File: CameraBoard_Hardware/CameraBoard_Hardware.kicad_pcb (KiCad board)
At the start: 2 copper layers, 61 x 100 mm, 39 parts, among them J1 CAM_OUT0, J2 CAM_OUT1, U1 TM4C129E_Launchpad, U2 AP1059, U3 MAX4314ESD+, U4 MAX4314ESD+

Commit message: Added BOM, added LED for +5V power
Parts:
- added D7: LED, LEDs:LED_0603_HandSoldering, F.Cu at (97.0, 97.1)
- added R14: 500, Resistors_SMD:R_0603_HandSoldering, F.Cu at (97.0, 104.3)
- J1: value CAM_OUT0 -> BNC_75_OHM_HORIZ
- J2: value CAM_OUT1 -> BNC_75_OHM_HORIZ
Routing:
- net +5V: track 100.4 -> 114.1 mm
- net Net-(D7-Pad1): track 0.00 -> 5.02 mm
- net GND: vias 3 -> 7
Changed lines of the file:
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@@
   (general
     (thickness 1.6)
-    (drawings 30)
-    (tracks 226)
+    (drawings 31)
+    (tracks 234)
     (zones 0)
-    (modules 39)
-    (nets 64)
+    (modules 41)
+    (nets 65)
   )
   (page A4)
@@
   )
   (setup
-    (last_trace_width 0.25)
+    (last_trace_width 0.381)
     (user_trace_width 0.254)
     (user_trace_width 0.381)
@@
   (net 62 "Net-(U1-Pad+3V3)")
   (net 63 +10V)
+  (net 64 "Net-(D7-Pad1)")
   (net_class Default "This is the default net class."
     (clearance 0.2)
@@
     (add_net "Net-(D5-Pad1)")
     (add_net "Net-(D6-Pad1)")
+    (add_net "Net-(D7-Pad1)")
     (add_net "Net-(J1-Pad2)")
     (add_net "Net-(J2-Pad2)")
@@
       (effects (font (size 1 1) (thickness 0.15)))
     )
-    (fp_text value CAM_OUT0 (at 2.3622 2.0828) (layer F.SilkS)
+    (fp_text value BNC_75_OHM_HORIZ (at 2.3622 2.0828) (layer F.SilkS)
       (effects (font (size 1 1) (thickness 0.15)))
     )
@@
       (effects (font (size 1 1) (thickness 0.15)))
     )
-    (fp_text value CAM_OUT1 (at 2.3876 2.0828) (layer F.SilkS)
+    (fp_text value BNC_75_OHM_HORIZ (at 2.3876 2.0828) (layer F.SilkS)
       (effects (font (size 1 1) (thickness 0.15)))
     )
@@
       (xy 3.076472 -5.52068) (xy 3.111284 -5.541334) (xy 3.12377 -5.541189)) (layer F.SilkS) (width 0.01))
   )
+  (module LEDs:LED_0603_HandSoldering (layer F.Cu)
+    (at 97.028 97.0866 90)
+    (descr "LED SMD 0603, hand soldering")
+    (tags "LED 0603")
+    (attr smd)
+    (fp_text reference D7 (at 2.9034 0 90) (layer F.SilkS)
+      (effects (font (size 1 1) (thickness 0.15)))
+    )
+    (fp_text value LED (at 0 1.55 90) (layer F.Fab)
+      (effects (font (size 1 1) (thickness 0.15)))
+    )
+    (fp_line (start -0.8 -0.4) (end -0.8 0.4) (layer F.Fab) (width 0.1))
+    (fp_line (start 1.95 0.7) (end -1.96 0.7) (layer F.CrtYd) (width 0.05))
+    (fp_line (start 1.95 0.7) (end 1.95 -0.7) (layer F.CrtYd) (width 0.05))
+    (fp_line (start -1.96 -0.7) (end -1.96 0.7) (layer F.CrtYd) (width 0.05))
+    (fp_line (start -1.96 -0.7) (end 1.95 -0.7) (layer F.CrtYd) (width 0.05))
+    (fp_line (start -1.8 -0.55) (end 0.8 -0.55) (layer F.SilkS) (width 0.12))
+    (fp_line (start -1.8 0.55) (end 0.8 0.55) (layer F.SilkS) (width 0.12))
+    (fp_line (start -0.8 -0.4) (end 0.8 -0.4) (layer F.Fab) (width 0.1))
+    (fp_line (start 0.8 -0.4) (end 0.8 0.4) (layer F.Fab) (width 0.1))
+    (fp_line (start 0.8 0.4) (end -0.8 0.4) (layer F.Fab) (width 0.1))
+    (fp_line (start 0.15 -0.2) (end 0.15 0.2) (layer F.Fab) (width 0.1))
+    (fp_line (start 0.15 0.2) (end -0.15 0) (layer F.Fab) (width 0.1))
+    (fp_line (start -0.15 0) (end 0.15 -0.2) (layer F.Fab) (width 0.1))
+    (fp_line (start -0.2 -0.2) (end -0.2 0.2) (layer F.Fab) (width 0.1))
+    (fp_line (start -1.8 -0.55) (end -1.8 0.55) (layer F.SilkS) (width 0.12))
+    (pad 2 smd rect (at 1.1 0 90) (size 1.2 0.9) (layers F.Cu F.Paste F.Mask)
+      (net 57 +5V))
+    (pad 1 smd rect (at -1.1 0 90) (size 1.2 0.9) (layers F.Cu F.Paste F.Mask)
+      (net 64 "Net-(D7-Pad1)"))
+    (model ${KISYS3DMOD}/LEDs.3dshapes/LED_0603.wrl
+      (at (xyz 0 0 0))
+      (scale (xyz 1 1 1))
+      (rotate (xyz 0 0 180))
+    )
+  )
+  (module Resistors_SMD:R_0603_HandSoldering (layer F.Cu)
+    (at 97.028 104.31 270)
+    (descr "Resistor SMD 0603, hand soldering")
+    (tags "resistor 0603")
+    (attr smd)
+    (fp_text reference R14 (at -3.3704 -0.0254 270) (layer F.SilkS)
+      (effects (font (size 1 1) (thickness 0.15)))
+    )
+    (fp_text value 500 (at 0 1.55 270) (layer F.Fab)
+      (effects (font (size 1 1) (thickness 0.15)))
+    )
+    (fp_line (start 1.95 0.7) (end -1.96 0.7) (layer F.CrtYd) (width 0.05))
+    (fp_line (start 1.95 0.7) (end 1.95 -0.7) (layer F.CrtYd) (width 0.05))
+    (fp_line (start -1.96 -0.7) (end -1.96 0.7) (layer F.CrtYd) (width 0.05))
+    (fp_line (start -1.96 -0.7) (end 1.95 -0.7) (layer F.CrtYd) (width 0.05))
+    (fp_line (start -0.5 -0.68) (end 0.5 -0.68) (layer F.SilkS) (width 0.12))
+    (fp_line (start 0.5 0.68) (end -0.5 0.68) (layer F.SilkS) (width 0.12))
+    (fp_line (start -0.8 -0.4) (end 0.8 -0.4) (layer F.Fab) (width 0.1))
+    (fp_line (start 0.8 -0.4) (end 0.8 0.4) (layer F.Fab) (width 0.1))
+    (fp_line (start 0.8 0.4) (end -0.8 0.4) (layer F.Fab) (width 0.1))
+    (fp_line (start -0.8 0.4) (end -0.8 -0.4) (layer F.Fab) (width 0.1))
+    (fp_text user %R (at 0 0 270) (layer F.Fab)
+      (effects (font (size 0.4 0.4) (thickness 0.075)))
+    )
+    (pad 2 smd rect (at 1.1 0 270) (size 1.2 0.9) (layers F.Cu F.Paste F.Mask)
+      (net 2 GND))
+    (pad 1 smd rect (at -1.1 0 270) (size 1.2 0.9) (layers F.Cu F.Paste F.Mask)
+      (net 64 "Net-(D7-Pad1)"))
+    (model ${KISYS3DMOD}/Resistors_SMD.3dshapes/R_0603.wrl
+      (at (xyz 0 0 0))
+      (scale (xyz 1 1 1))
+      (rotate (xyz 0 0 0))
+    )
+  )
+  (gr_text +5V (at 97.0788 107.9754 90) (layer F.SilkS)
+    (effects (font (size 1 1) (thickness 0.15)))
+  )
   (gr_text +10V (at 127.0254 62.23) (layer F.SilkS)
     (effects (font (size 1.5 1.5) (thickness 0.3)))
@@
   (segment (start 126.2736 101.3968) (end 126.2736 101.2088) (width 0.381) (layer F.Cu) (net 2))
   (via (at 124.6378 99.3648) (size 0.8) (drill 0.4) (layers F.Cu B.Cu) (net 2))
+  (via (at 100.1268 101.2698) (size 0.8) (drill 0.4) (layers F.Cu B.Cu) (net 2))
+  (via (at 101.4476 102.6668) (size 0.8) (drill 0.4) (layers F.Cu B.Cu) (net 2))
+  (via (at 103.4288 100.3554) (size 0.8) (drill 0.4) (layers F.Cu B.Cu) (net 2))
+  (via (at 102.2858 99.1616) (size 0.8) (drill 0.4) (layers F.Cu B.Cu) (net 2))
   (via (at 130.4544 91.8972) (size 0.8) (drill 0.4) (layers F.Cu B.Cu) (net 3))
   (segment (start 127.0762 91.9226) (end 130.429 91.9226) (width 0.381) (layer F.Cu) (net 3))
@@
   (segment (start 106.8578 105.3338) (end 121.793 105.3338) (width 0.381) (layer B.Cu) (net 57))
   (segment (start 106.4006 105.791) (end 106.8578 105.3338) (width 0.381) (layer B.Cu) (net 57))
+  (segment (start 106.4006 105.5092) (end 106.4006 105.791) (width 0.381) (layer F.Cu) (net 57))
+  (segment (start 97.028 96.1366) (end 106.4006 105.5092) (width 0.381) (layer F.Cu) (net 57))
+  (segment (start 97.028 95.9866) (end 97.028 96.1366) (width 0.381) (layer F.Cu) (net 57))
   (segment (start 125.5014 60.198) (end 124.587 59.2836) (width 0.381) (layer F.Cu) (net 58))
   (segment (start 125.5014 64.9224) (end 125.5014 60.198) (width 0.381) (layer F.Cu) (net 58))
@@
   (segment (start 115.6716 105.3182) (end 115.6462 105.3436) (width 0.381) (layer F.Cu) (net 63))
   (segment (start 115.6716 101.0666) (end 115.6716 105.3182) (width 0.381) (layer F.Cu) (net 63))
+  (segment (start 97.028 98.1866) (end 97.028 103.21) (width 0.381) (layer F.Cu) (net 64))
   (zone (net 2) (net_name GND) (layer F.Cu) (hatch edge 0.508)
     (connect_pads yes (clearance 0.508))

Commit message: Re-Routed Traces
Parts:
- removed CAM_IN0: CAM_0, MRDT_Connectors:MOLEX_SL_03_Horizontal
- removed CAM_IN1: CAM_1, MRDT_Connectors:MOLEX_SL_03_Horizontal
- removed CAM_IN2: CAM_2, MRDT_Connectors:MOLEX_SL_03_Horizontal
- removed CAM_IN3: CAM_3, MRDT_Connectors:MOLEX_SL_03_Horizontal
- removed JP2: Jumper_NC_Dual, Pin_Headers:Pin_Header_Straight_1x03_Pitch2.54mm
- added Conn3: CAM_0, MRDT_Connectors:MOLEX_SL_03_Horizontal, F.Cu at (134.6, 99.1)
- added Conn4: CAM_1, MRDT_Connectors:MOLEX_SL_03_Horizontal, F.Cu at (134.6, 86.4)
- added Conn5: CAM_2, MRDT_Connectors:MOLEX_SL_03_Horizontal, F.Cu at (134.6, 73.7)
- added Conn6: CAM_3, MRDT_Connectors:MOLEX_SL_03_Horizontal, F.Cu at (134.6, 61.0)
- L1: footprint Inductors_SMD:L_0603_HandSoldering -> MRDT_Passives:DR74_330_R
- moved JP1 36.0 mm to (126.2, 95.2)
- moved R13 13.1 mm to (125.1, 99.3), turned to 180 degrees
- moved R12 12.7 mm to (127.3, 101.6), turned to 180 degrees
- moved C4 9.20 mm to (125.5, 92.2), turned to 180 degrees
- moved U4 6.87 mm to (123.9, 86.4)
- moved R7 6.38 mm to (133.2, 78.7), turned to 180 degrees
- moved R8 5.61 mm to (133.2, 66.0), turned to 180 degrees
- moved L1 4.47 mm to (107.0, 106.7)
- moved C1 4.25 mm to (111.5, 116.3)
- moved D5 4.23 mm to (108.8, 112.5)
- moved R14 4.22 mm to (100.3, 101.7)
- moved C2 4.18 mm to (105.0, 112.5), turned to 0 degrees
- moved R3 4.16 mm to (95.2, 101.7)
- moved R2 3.85 mm to (87.6, 101.7)
- moved R11 3.59 mm to (97.8, 101.7)
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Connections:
- C3 pad 1: Net-(C3-Pad1) -> /MUX_PWR
- C4 pad 1: Net-(C4-Pad1) -> /MUX_PWR
- JP1 pad 2: Net-(C3-Pad1) -> /MUX_PWR
- U1 pad +3V3: Net-(U1-Pad+3V3) -> (no net)
- U1 pad PA6: Net-(U1-PadPA6) -> (no net)
- U1 pad PB2: Net-(U1-PadPB2) -> (no net)
- U1 pad PB3: Net-(U1-PadPB3) -> (no net)
- U1 pad PC4: Net-(U1-PadPC4) -> (no net)
- U1 pad PC5: Net-(U1-PadPC5) -> (no net)
- U1 pad PC6: Net-(U1-PadPC6) -> (no net)
- U1 pad PC7: Net-(U1-PadPC7) -> (no net)
- U1 pad PD0: MUXA_SHDN -> (no net)
- U1 pad PD1: MUXB_SHDN -> (no net)
- U1 pad PD3: Net-(U1-PadPD3) -> (no net)
- U1 pad PD7: Net-(U1-PadPD7) -> (no net)
- U1 pad PE0: Net-(U1-PadPE0) -> (no net)
- U1 pad PE1: Net-(U1-PadPE1) -> (no net)
- U1 pad PE2: Net-(U1-PadPE2) -> (no net)
- U1 pad PE3: Net-(U1-PadPE3) -> (no net)
- U1 pad PE4: Net-(U1-PadPE4) -> (no net)
- U1 pad PE5: Net-(U1-PadPE5) -> (no net)
- U1 pad PF1: MUXA1 -> MUXA0
- U1 pad PF2: MUXA0 -> MUXA1
- U1 pad PF3: MUXB1 -> MUXB0
- U1 pad PG0: MUXB0 -> MUXB1
- U1 pad PH2: Net-(U1-PadPH2) -> (no net)
- U1 pad PH3: Net-(U1-PadPH3) -> (no net)
- U1 pad PL0: Net-(U1-PadPL0) -> (no net)
- U1 pad PL1: Net-(U1-PadPL1) -> (no net)
- U1 pad PL2: Net-(U1-PadPL2) -> (no net)
- U1 pad PL3: Net-(U1-PadPL3) -> MUXB_SHDN
- U1 pad PL4: Net-(U1-PadPL4) -> SW_ERR
- U1 pad PL5: Net-(U1-PadPL5) -> (no net)
- U1 pad PM3: Net-(U1-PadPM3) -> (no net)
- U1 pad PM4: Net-(U1-PadPM4) -> (no net)
- U1 pad PM5: Net-(U1-PadPM5) -> (no net)
- U1 pad PN2: Net-(U1-PadPN2) -> (no net)
- U1 pad PN3: Net-(U1-PadPN3) -> (no net)
- U1 pad PP2: SW_ERR -> MUXA_SHDN
- U1 pad Rese: Net-(U1-PadRese) -> (no net)
- U3 pad 3: Net-(U3-Pad3) -> (no net)
- U3 pad 4: Net-(C3-Pad1) -> /MUX_PWR
- U3 pad 6: Net-(U3-Pad6) -> (no net)
- U3 pad 9: Net-(U3-Pad9) -> (no net)
- U4 pad 3: Net-(U4-Pad3) -> (no net)
- U4 pad 4: Net-(C4-Pad1) -> /MUX_PWR
- U4 pad 6: Net-(U4-Pad6) -> (no net)
- U4 pad 9: Net-(U4-Pad9) -> (no net)
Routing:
- net +10V: track 75.9 -> 6.35 mm, vias 1 -> 0
- net +5V: track 114.1 -> 44.7 mm, vias 1 -> 0
- net /MUX_PWR: track 0.00 -> 40.8 mm, vias 0 -> 4
- net CAM_OUT1: track 37.4 -> 0.00 mm, vias 2 -> 0
- net +12V: track 92.3 -> 111.3 mm, vias 1 -> 0
- net SW_ERR: track 26.7 -> 10.3 mm
- net MUXB_SHDN: track 32.4 -> 16.4 mm, vias 1 -> 0
- net Net-(C4-Pad1): track 15.9 -> 0.00 mm
- net Net-(C3-Pad1): track 14.4 -> 0.00 mm
- net MUXB1: track 63.9 -> 52.1 mm, vias 2 -> 0
- net CAM_IN0: track 38.8 -> 48.6 mm, vias 3 -> 4
- net MUXA_SHDN: track 25.4 -> 17.2 mm
- net CAM_IN2: track 46.5 -> 41.1 mm, vias 3 -> 2
- net GND: track 4.32 -> 0.00 mm, vias 7 -> 0
- net Net-(D5-Pad1): track 6.27 -> 10.5 mm
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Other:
- board outline removed
- board text added: "Out 0"
- board text added: "Out 1"
- board text removed: "+10V"

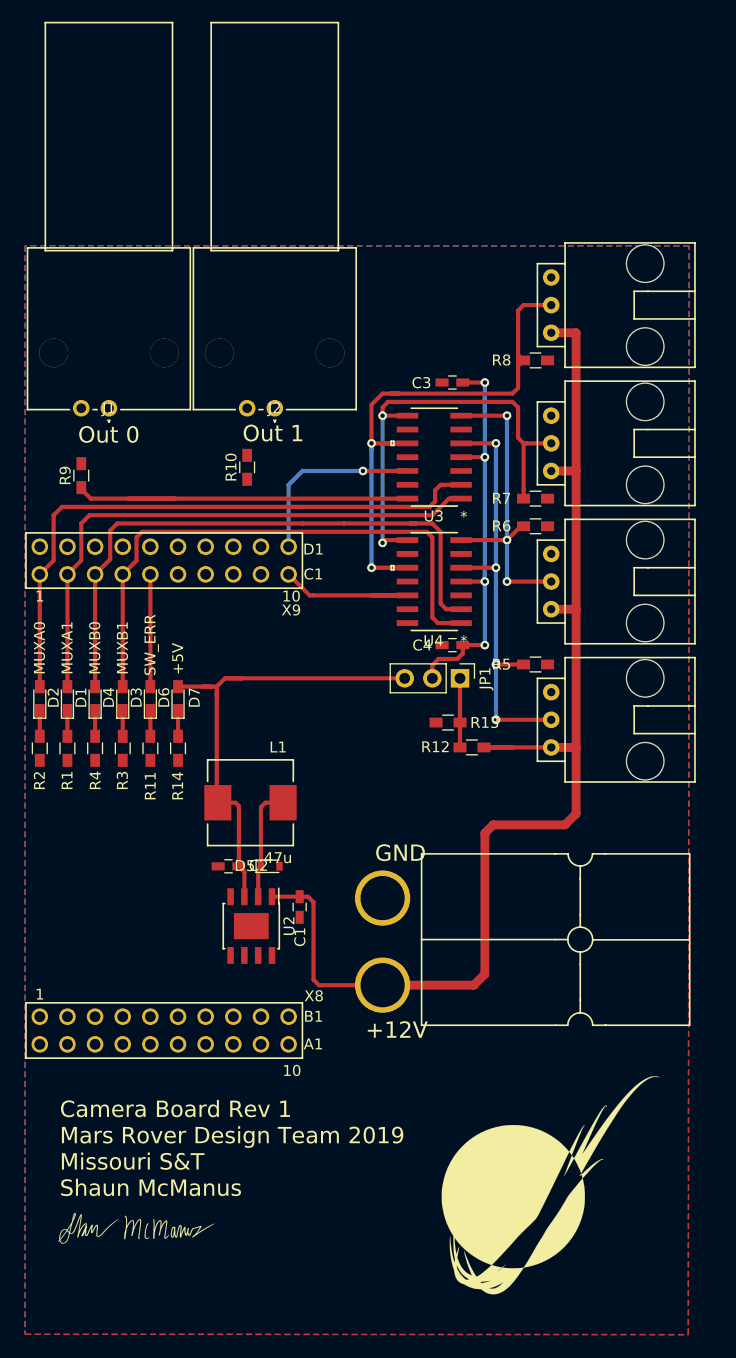
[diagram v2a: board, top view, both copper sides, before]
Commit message: finished silkscreen.
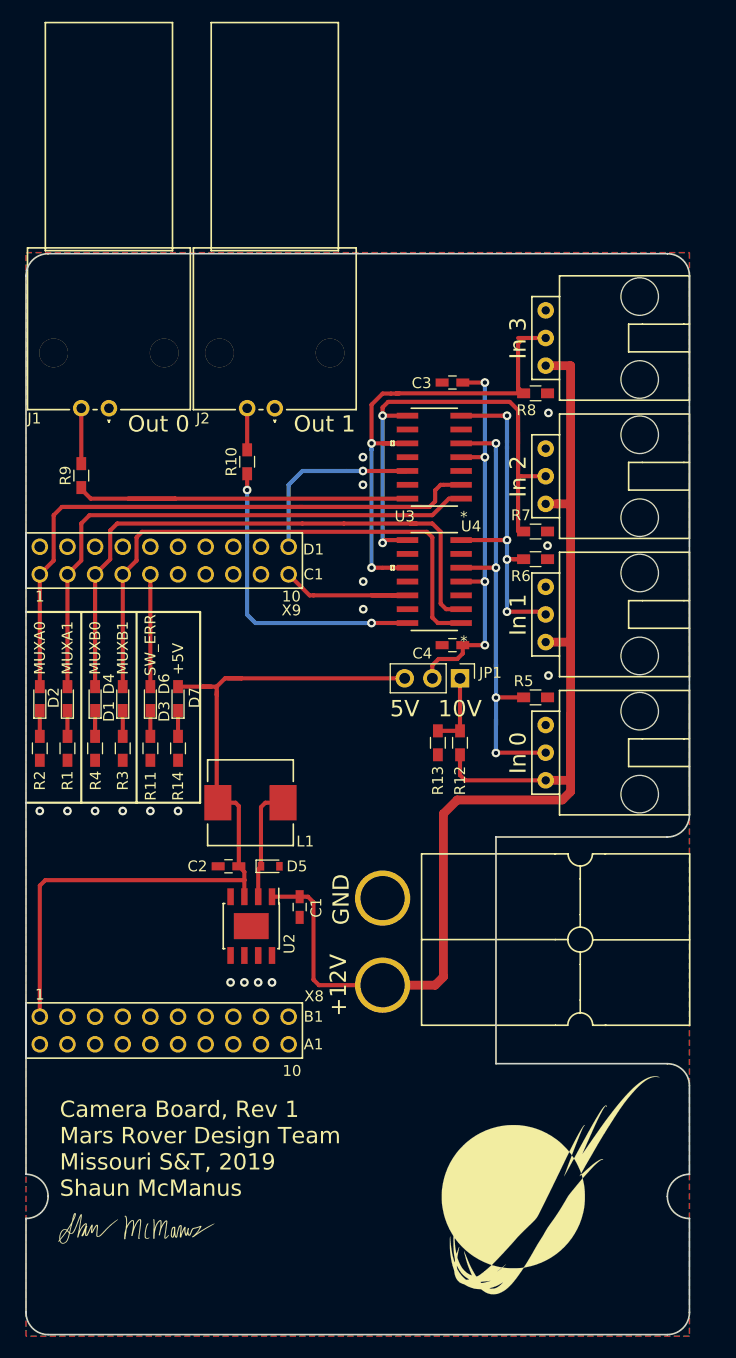
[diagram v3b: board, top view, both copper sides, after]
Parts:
- moved Conn3 3.06 mm to (134.1, 102.1)
- moved Conn4 3.06 mm to (134.1, 89.4)
- moved Conn5 3.06 mm to (134.1, 76.7)
- moved Conn6 3.06 mm to (134.1, 64.0)
- moved R7 3.02 mm to (133.2, 81.8)
- moved R5 3.02 mm to (133.2, 97.0)
- moved R6 3.02 mm to (133.2, 84.3)
- moved R8 3.02 mm to (133.2, 69.1)
- moved R13 2.08 mm to (124.2, 101.2), turned to 270 degrees
- moved R12 1.18 mm to (126.2, 101.2), turned to 90 degrees
- moved R10 0.51 mm to (106.7, 75.4)
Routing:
- net +5V: track 44.7 -> 75.8 mm
- net CAM_OUT1: track 0.00 -> 29.0 mm, vias 0 -> 2
- net Net-(J1-Pad2): track 0.00 -> 5.09 mm
- net CAM_IN2: track 41.1 -> 45.6 mm
- net +12V: track 111.3 -> 115.4 mm
- net CAM_IN1: track 29.8 -> 33.8 mm, vias 3 -> 4
- net CAM_IN3: track 50.6 -> 46.6 mm
- net Net-(J2-Pad2): track 0.00 -> 3.82 mm
- net CAM_IN0: track 48.6 -> 51.9 mm
- net +10V: track 6.35 -> 6.86 mm
- net GND: vias 0 -> 17
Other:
- board outline added: 61 x 99.3 mm
- board text added: "+12"
- board text added: "10V"
- board text added: "5V"
- board text added: "Camera Board, Rev 1 Mars Rover Design Team Missouri S&T, 2019 Shaun McManus"
- board text added: "G"
- board text added: "In 0"
- board text added: "In 1"
- board text added: "In 2"
- board text added: "In 3"
- board text added: "S"
- board text removed: "Camera Board Rev 1 Mars Rover Design Team 2019 Missouri S&T Shaun McManus"

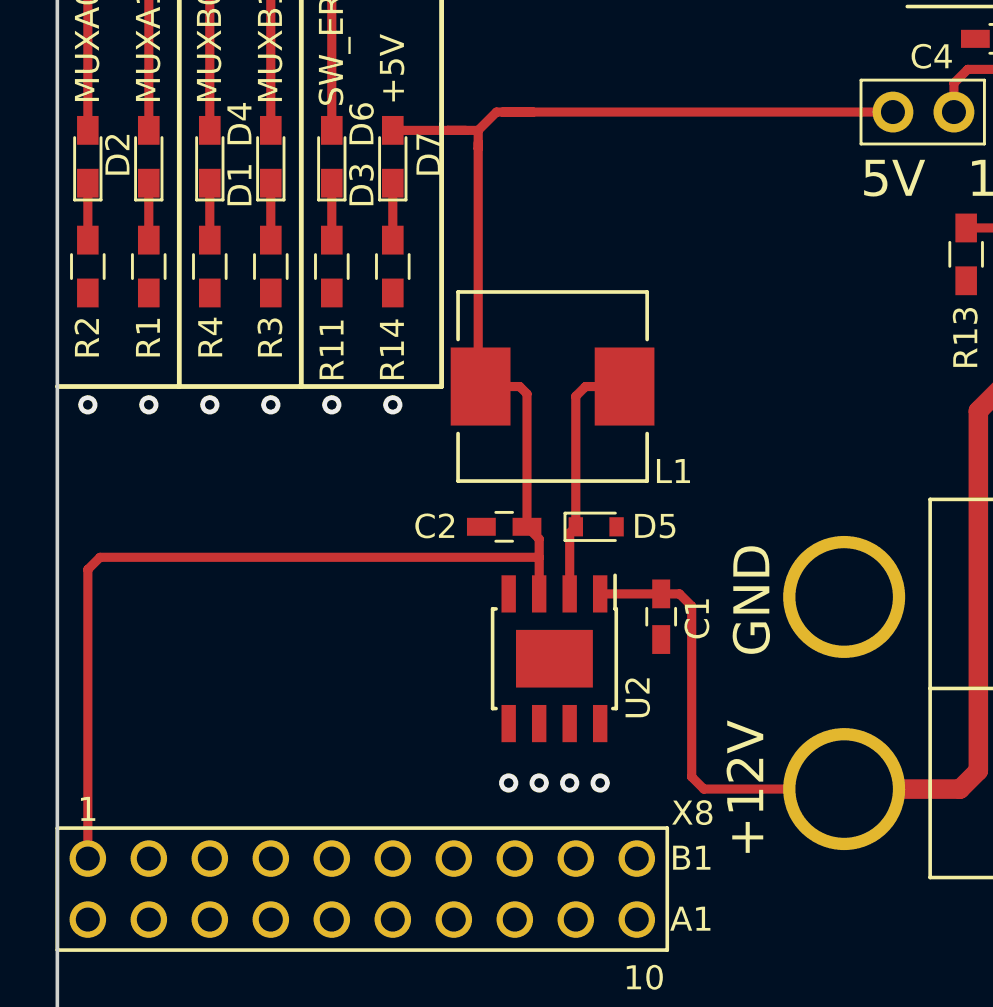
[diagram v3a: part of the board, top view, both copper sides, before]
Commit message: Updates Power Conversion
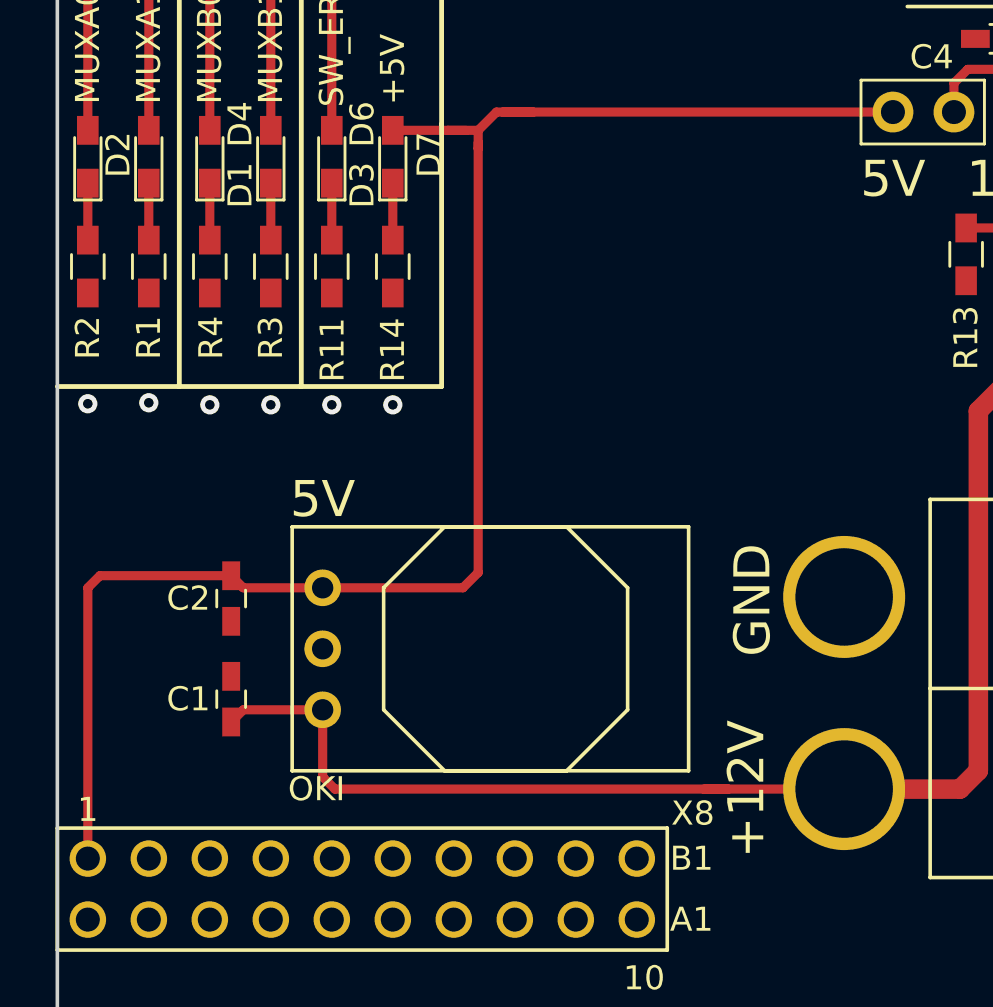
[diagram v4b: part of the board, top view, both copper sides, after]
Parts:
- removed D5: D_Schottky, Diodes_SMD:D_0603
- removed L1: 47u, MRDT_Passives:DR74_330_R
- C1, C2: value 10u -> 10uF
- U2: value AP1059 -> OKI; footprint Housings_SOIC:HTSOP-8-1EP_3.9x4.9mm_Pitch1.27mm -> MRDT_Devices:OKI_Horizontal
- moved C1 18.2 mm to (93.6, 119.7), turned to 90 degrees
- moved U2 11.9 mm to (96.1, 122.7), turned to 90 degrees
- moved C2 11.8 mm to (93.6, 115.5), turned to 270 degrees
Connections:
- C2 pad 1: GND -> +5V
- C2 pad 2: +5V -> GND
- U2 pad 2: Net-(D5-Pad1) -> GND
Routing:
- net +12V: track 115.4 -> 127.5 mm
- net Net-(D5-Pad1): track 10.5 -> 0.00 mm
- net +5V: track 75.8 -> 70.1 mm, vias 0 -> 7
- net GND: vias 17 -> 6
